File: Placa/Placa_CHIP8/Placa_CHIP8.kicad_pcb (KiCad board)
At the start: 2 copper layers, 101 x 72 mm, 11 parts, among them J1 Conn_01x08_Male-Teclado-Matri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, J2 Conn_01x06_Female-SD, J3 Conn_01x20_Female_LCD, J4 Conn_01x03_Male-UART, Q1 BC337, U1 STM32F103C8Tx, U2 Fuente

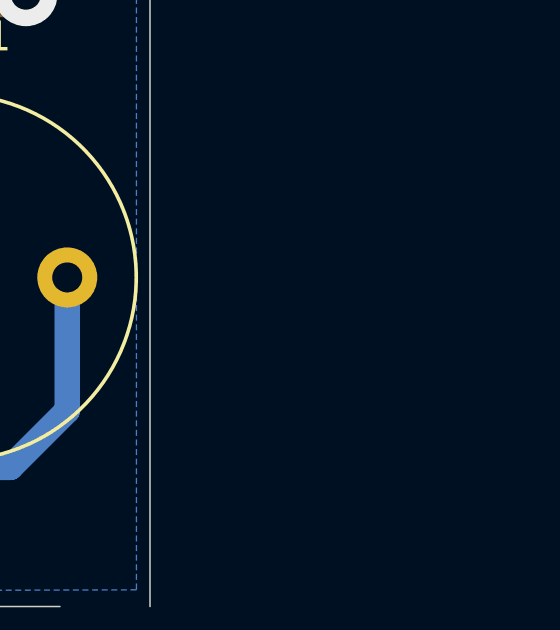
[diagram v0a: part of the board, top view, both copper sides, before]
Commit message: Modifico Placa con las conexiones nuevas
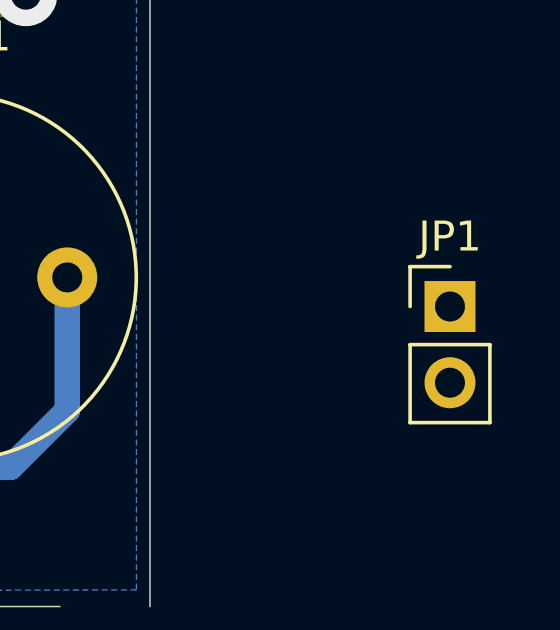
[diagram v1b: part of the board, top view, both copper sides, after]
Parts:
- added JP1: Jumper, Connector_PinHeader_2.54mm:PinHeader_1x02_P2.54mm_Vertical, F.Cu at (204.0, 114.0)
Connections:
- net /CLK renamed /SD_CLK
- net /CS renamed /SD_CS
- net /LCD_4 renamed /LCD_RST
- net /MISO renamed /SD_MISO
- net /MOSI renamed /SD_MOSI
- J3 pad 4: /LCD_1 -> /LCD_CS
- J3 pad 5: /LCD_2 -> /LCD_MOSI
- J3 pad 6: /LCD_3 -> /LCD_CLK
- R1 pad 2: /Buzzer -> Net-(JP1-Pad2)
- U1 pad 21: Net-(U1-Pad21) -> /LCD_CS
- U1 pad 22: (no net) -> /LCD_CLK
- U1 pad 24: Net-(U1-Pad24) -> /LCD_MOSI
- U1 pad 5: /LCD_3 -> Net-(U1-Pad5)
- U1 pad 6: /LCD_1 -> Net-(U1-Pad6)
- U1 pad 7: /LCD_2 -> Net-(U1-Pad7)

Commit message: Agrego modelo Willy funcando ok y V1 gabinete
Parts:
- JP1: footprint Connector_PinHeader_2.54mm:PinHeader_1x02_P2.54mm_Vertical -> Connector_PinHeader_2.54mm:PinHeader_1x03_P2.54mm_Vertical
- moved BZ1 77.1 mm to (106.7, 118.1)
- moved JP1 69.4 mm to (134.6, 113.0), turned to 270 degrees
- moved J2 47.3 mm to (160.0, 78.7), turned to 180 degrees
- moved J4 46.9 mm to (147.3, 113.0), turned to 270 degrees
- moved Q1 36.2 mm to (120.7, 119.4), turned to 90 degrees
- moved U2 31.6 mm to (121.9, 109.2), turned to 90 degrees
- moved R1 31.2 mm to (124.5, 116.8), turned to 0 degrees
- moved U1 22.4 mm to (177.8, 91.4)
- moved BT1 19.5 mm to (135.9, 83.8), turned to 90 degrees
- moved J1 8.70 mm to (170.2, 113.0)
- moved J3 1.91 mm to (123.2, 55.9)
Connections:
- J4 pad 2: /TX_1 -> /RX_1
- J4 pad 3: /RX_1 -> /TX_1
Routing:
- net GND: track 71.2 -> 398.5 mm, vias 8 -> 0
- net /LCD_MOSI: track 0.00 -> 64.0 mm, vias 0 -> 2
- net /TX_1: track 64.9 -> 6.59 mm, vias 2 -> 0
- net /LCD_1: track 57.9 -> 0.00 mm
- net /LCD_CS: track 0.00 -> 57.9 mm
- net /LCD_CLK: track 0.00 -> 57.4 mm
- net /LCD_3: track 54.3 -> 0.00 mm
- net /LCD_2: track 52.8 -> 0.00 mm, vias 2 -> 0
- net /SD_CLK: track 76.7 -> 24.7 mm, vias 2 -> 0
- net /SD_MISO: track 79.8 -> 29.7 mm
- net /SD_CS: track 65.1 -> 17.0 mm, vias 2 -> 0
- net /RX_1: track 49.8 -> 6.59 mm, vias 2 -> 0
- net +3V3: track 183.6 -> 145.3 mm, vias 2 -> 4
- net /SD_MOSI: track 64.1 -> 27.9 mm, vias 0 -> 2
- net Net-(BZ1-Pad2): track 41.3 -> 6.98 mm
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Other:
- board outline removed

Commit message: Mejoras minimas codigo
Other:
- board outline added: 98 x 75 mm
